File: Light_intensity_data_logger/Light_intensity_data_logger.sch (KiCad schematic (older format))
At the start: 12 parts

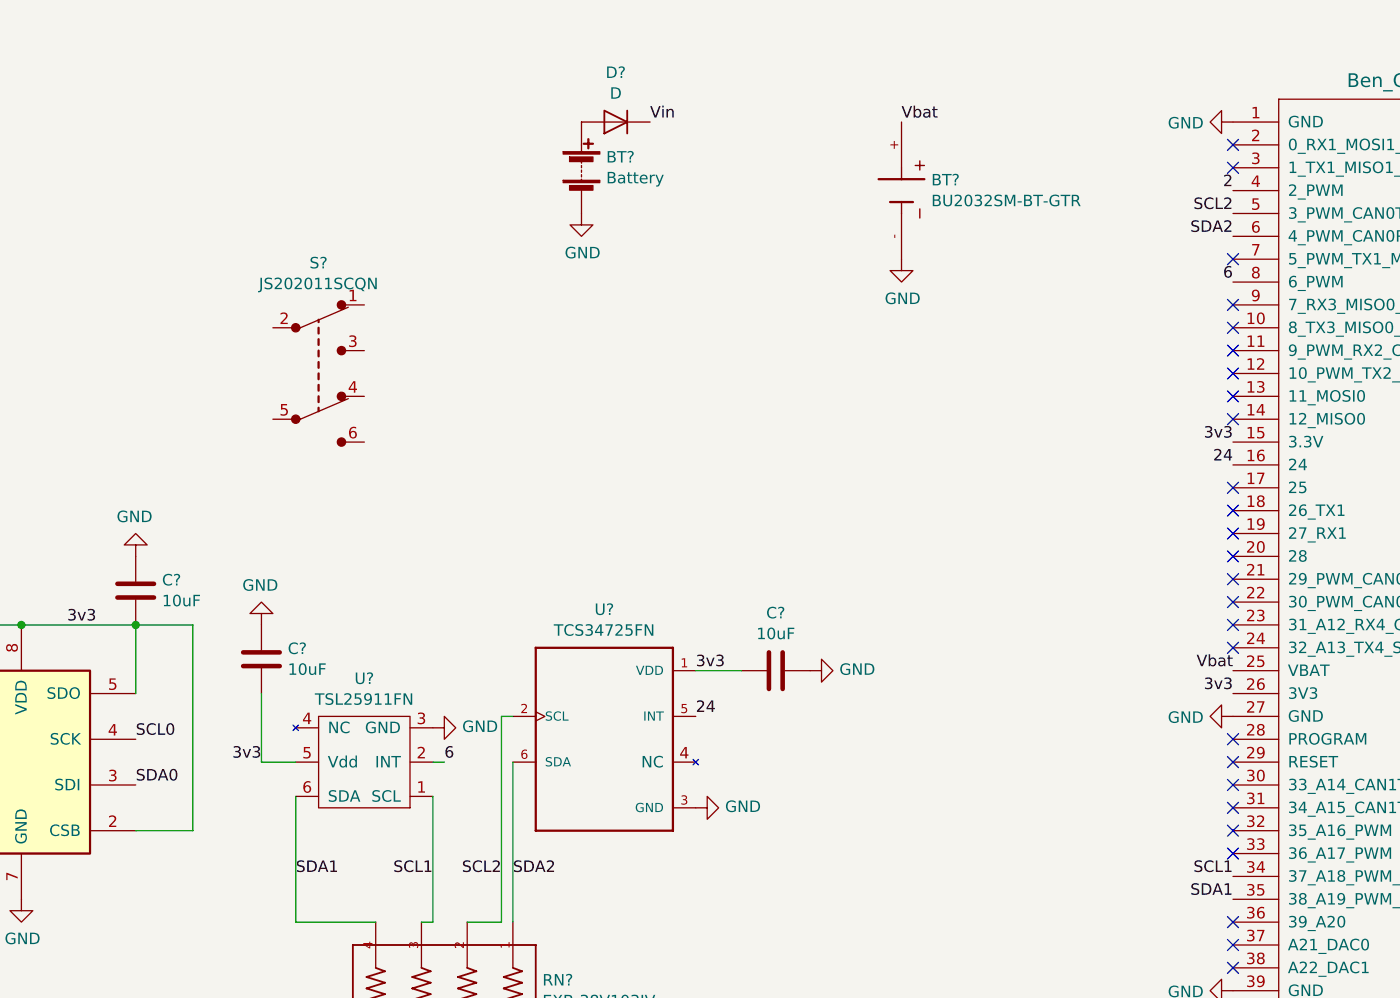
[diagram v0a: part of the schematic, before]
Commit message: Add power switch and Vbat sense
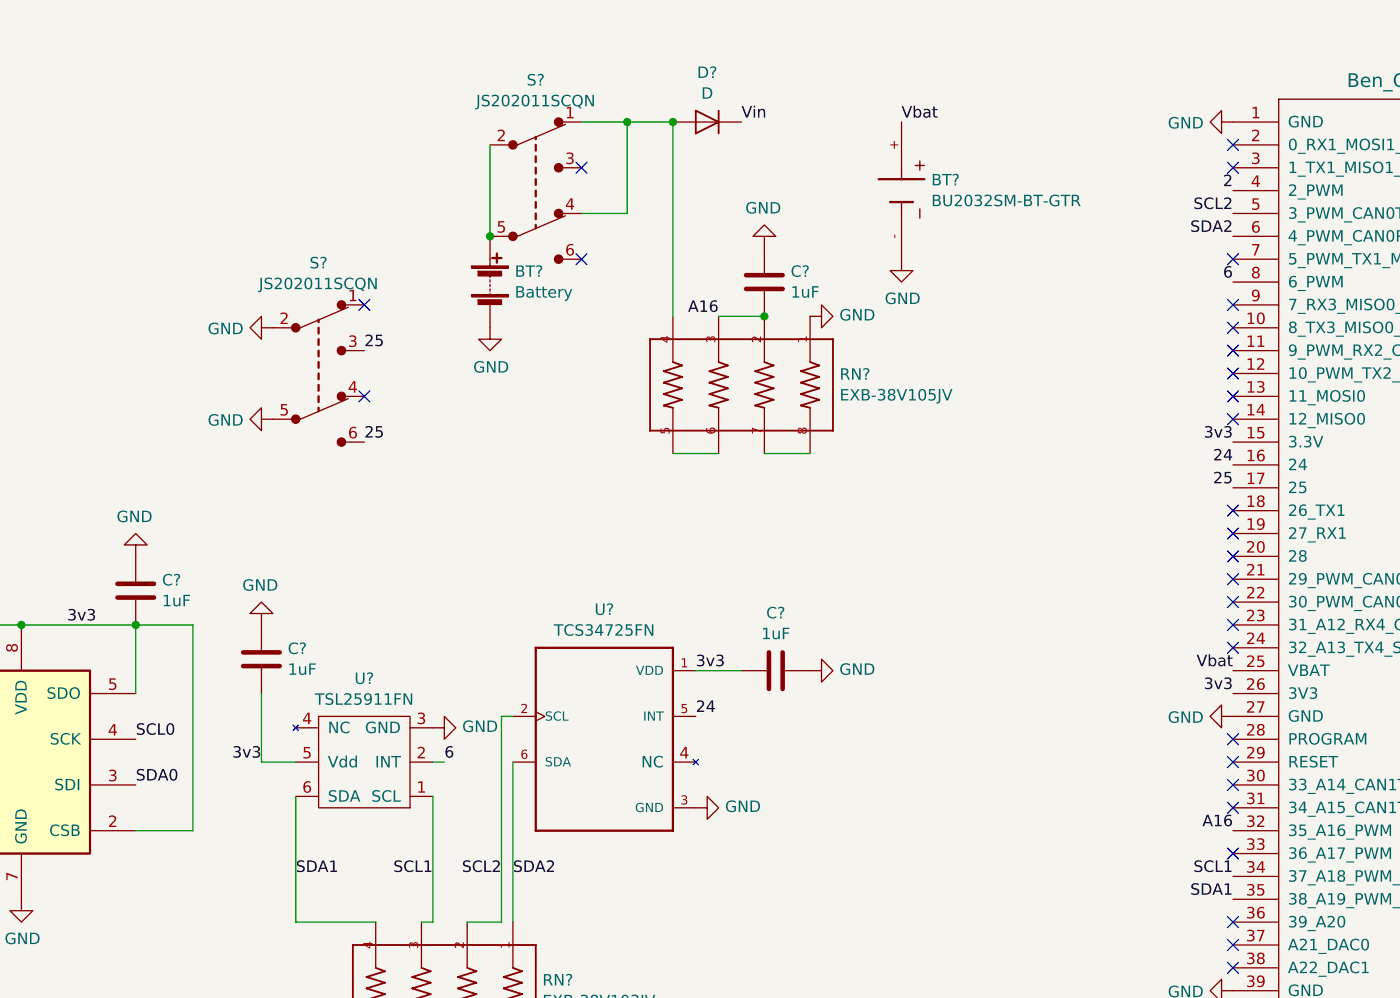
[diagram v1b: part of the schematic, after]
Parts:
- removed C? (x2): 10uF, Ben_Custom:0508_Capacitor, symbol device:C
- added C? (x3): 1uF, Capacitors_SMD:C_0603, symbol device:C
- added RN?: EXB-38V105JV, RESCAXS80P320X160X60-8N, symbol Ben_custom:EXB-38V103JV
- added S?: JS202011SCQN, digikey-footprints:Switch_Slide_JS202011SCQN, symbol dk_Slide-Switches:JS202011SCQN
- C?: value 10uF -> 1uF; footprint Ben_Custom:0508_Capacitor -> Capacitors_SMD:C_0603; Part# 587-5164-1-ND -> 1276-6524-1-ND
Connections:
- net 3v3: now also C?.2, C?.2
- net GND: now also S?.2, S?.5, C?.1, C?.1, C?.2, RN?.1
- net 25: now reaches U?.17 (25)
- net 25: now also S?.3, S?.6
- net A16: now reaches U?.32 (35_A16_PWM)
- net A16: now also C?.1, RN?.2, RN?.3
- net at BT?.1 (+): now also S?.2, S?.5; no longer D?.2 (A)
- new net: D?.2 (A), RN?.4, S?.1, S?.4
- new net: RN?.5, RN?.6
- new net: RN?.7, RN?.8
- no-connect marks 69 -> 71
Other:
- moved on the sheet: BT?, D?
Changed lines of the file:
@@
 L device:Battery BT?
 U 1 1 5E1E70C1
-P 5800 1050
-F 0 "BT?" H 5908 1096 50  0000 L CNN
-F 1 "Battery" H 5908 1005 50  0000 L CNN
-F 2 "Ben_Custom:BH3AAW-Battery_wire_pads" V 5800 1110 50  0001 C CNN
-F 3 "http://www.memoryprotectiondevices.com/datasheets/BH3AAW-datasheet.pdf" V 5800 1110 50  0001 C CNN
-F 4 "BH3AA-W-ND" H 5800 1050 50  0001 C CNN "Part#"
-	1    5800 1050
+P 5400 1550
+F 0 "BT?" H 5508 1596 50  0000 L CNN
+F 1 "Battery" H 5508 1505 50  0000 L CNN
+F 2 "Ben_Custom:BH3AAW-Battery_wire_pads" V 5400 1610 50  0001 C CNN
+F 3 "http://www.memoryprotectiondevices.com/datasheets/BH3AAW-datasheet.pdf" V 5400 1610 50  0001 C CNN
+F 4 "BH3AA-W-ND" H 5400 1550 50  0001 C CNN "Part#"
+	1    5400 1550
 	1    0    0    -1
 $EndComp
 Text Label 10950 4350 0    50   ~ 0
 Vin
-Text Label 6100 850  0    50   ~ 0
+Text Label 6500 850  0    50   ~ 0
 Vin
 $Comp
 L power:GND #PWR?
 U 1 1 5E1EC268
-P 5800 1250
-F 0 "#PWR?" H 5800 1000 50  0001 C CNN
-F 1 "GND" H 5805 1077 50  0000 C CNN
-F 2 "" H 5800 1250 50  0001 C CNN
-F 3 "" H 5800 1250 50  0001 C CNN
-	1    5800 1250
+P 5400 1750
+F 0 "#PWR?" H 5400 1500 50  0001 C CNN
+F 1 "GND" H 5405 1577 50  0000 C CNN
+F 2 "" H 5400 1750 50  0001 C CNN
+F 3 "" H 5400 1750 50  0001 C CNN
+	1    5400 1750
 	1    0    0    -1
 $EndComp
@@
 L device:D D?
 U 1 1 5E1F5931
-P 5950 850
-F 0 "D?" H 5950 634 50  0000 C CNN
-F 1 "D" H 5950 725 50  0000 C CNN
-F 2 "Diodes_SMD:D_SOD-323" H 5950 850 50  0001 C CNN
-F 3 "https://toshiba.semicon-storage.com/info/docget.jsp?did=14077&prodName=CUS10S30" H 5950 850 50  0001 C CNN
-F 4 "CUS10S30H3FCT-ND" H 5950 850 50  0001 C CNN "Part#"
-	1    5950 850
+P 6350 850
+F 0 "D?" H 6350 634 50  0000 C CNN
+F 1 "D" H 6350 725 50  0000 C CNN
+F 2 "Diodes_SMD:D_SOD-323" H 6350 850 50  0001 C CNN
+F 3 "https://toshiba.semicon-storage.com/info/docget.jsp?did=14077&prodName=CUS10S30" H 6350 850 50  0001 C CNN
+F 4 "CUS10S30H3FCT-ND" H 6350 850 50  0001 C CNN "Part#"
+	1    6350 850
 	-1   0    0    1
 $EndComp
@@
 F 1 "BME280" H 2821 3605 50  0000 R CNN
 F 2 "Housings_LGA:LGA-8_2.5x2.5mm_Pitch0.65mm" H 3250 3450 50  0001 C CNN
-F 3 "https://ae-bst.resource.bosch.com/media/_tech/media/datasheets/BST-BME280_DS001-11.pdf" H 3250 3450 50  0001 C CNN
+F 3 "https://www.bosch-sensortec.com/media/boschsensortec/downloads/environmental_sensors_2/humidity_sensors_1/bme280/bst-bme280-ds002.pdf" H 3250 3450 50  0001 C CNN
 F 4 "828-1063-1-ND" H 3250 3650 50  0001 C CNN "Part#"
 	1    3250 3650
@@
 NoConn ~ 8650 2050
 NoConn ~ 8650 2150
-NoConn ~ 8650 2450
 NoConn ~ 8650 2550
 NoConn ~ 8650 2650
@@
 NoConn ~ 8650 3750
 NoConn ~ 8650 3850
-NoConn ~ 8650 3950
 NoConn ~ 8650 4050
 NoConn ~ 8650 4350
@@
 P 3850 2900
 F 0 "C?" H 3965 2946 50  0000 L CNN
-F 1 "10uF" H 3965 2855 50  0000 L CNN
-F 2 "Ben_Custom:0508_Capacitor" H 3888 2750 50  0001 C CNN
-F 3 "https://media.digikey.com/pdf/Data%20Sheets/Taiyo%20Yuden%20PDFs%20URL%20links/EWK212BJ106MD-T_Spec.pdf" H 3850 2900 50  0001 C CNN
-F 4 "587-5164-1-ND" H 3850 2900 50  0001 C CNN "Part#"
+F 1 "1uF" H 3965 2855 50  0000 L CNN
+F 2 "Capacitors_SMD:C_0603" H 3888 2750 50  0001 C CNN
+F 3 "https://media.digikey.com/pdf/Data%20Sheets/Samsung%20PDFs/CL10B105MO8NNWC.pdf" H 3850 2900 50  0001 C CNN
+F 4 "1276-6524-1-ND" H 3850 2900 50  0001 C CNN "Part#"
 	1    3850 2900
 	1    0    0    -1
@@
 	-1   0    0    1
 $EndComp
-$Comp
-L device:C C?
-U 1 1 5E23E072
-P 4400 3200
-F 0 "C?" H 4515 3246 50  0000 L CNN
-F 1 "10uF" H 4515 3155 50  0000 L CNN
-F 2 "Ben_Custom:0508_Capacitor" H 4438 3050 50  0001 C CNN
-F 3 "https://media.digikey.com/pdf/Data%20Sheets/Taiyo%20Yuden%20PDFs%20URL%20links/EWK212BJ106MD-T_Spec.pdf" H 4400 3200 50  0001 C CNN
-F 4 "587-5164-1-ND" H 4400 3200 50  0001 C CNN "Part#"
-	1    4400 3200
-	1    0    0    -1
-$EndComp
 Wire Wire Line
 	4550 3650 4400 3650
@@
 	1    4400 3050
 	-1   0    0    1
-$EndComp
-$Comp
-L device:C C?
-U 1 1 5E23FF0F
-P 6650 3250
-F 0 "C?" V 6398 3250 50  0000 C CNN
-F 1 "10uF" V 6489 3250 50  0000 C CNN
-F 2 "Ben_Custom:0508_Capacitor" H 6688 3100 50  0001 C CNN
-F 3 "https://media.digikey.com/pdf/Data%20Sheets/Taiyo%20Yuden%20PDFs%20URL%20links/EWK212BJ106MD-T_Spec.pdf" H 6650 3250 50  0001 C CNN
-F 4 "587-5164-1-ND" H 6650 3250 50  0001 C CNN "Part#"
-	1    6650 3250
-	0    1    1    0
 $EndComp
 Wire Wire Line
@@
 Wire Wire Line
 	4100 3950 3850 3950
+$Comp
+L device:C C?
+U 1 1 5E24F840
+P 4400 3200
+F 0 "C?" H 4515 3246 50  0000 L CNN
+F 1 "1uF" H 4515 3155 50  0000 L CNN
+F 2 "Capacitors_SMD:C_0603" H 4438 3050 50  0001 C CNN
+F 3 "https://media.digikey.com/pdf/Data%20Sheets/Samsung%20PDFs/CL10B105MO8NNWC.pdf" H 4400 3200 50  0001 C CNN
+F 4 "1276-6524-1-ND" H 4400 3200 50  0001 C CNN "Part#"
+	1    4400 3200
+	1    0    0    -1
+$EndComp
+$Comp
+L device:C C?
+U 1 1 5E24FD3B
+P 6650 3250
+F 0 "C?" V 6398 3250 50  0000 C CNN
+F 1 "1uF" V 6489 3250 50  0000 C CNN
+F 2 "Capacitors_SMD:C_0603" H 6688 3100 50  0001 C CNN
+F 3 "https://media.digikey.com/pdf/Data%20Sheets/Samsung%20PDFs/CL10B105MO8NNWC.pdf" H 6650 3250 50  0001 C CNN
+F 4 "1276-6524-1-ND" H 6650 3250 50  0001 C CNN "Part#"
+	1    6650 3250
+	0    1    1    0
+$EndComp
+$Comp
+L Ben_custom:EXB-38V103JV RN?
+U 1 1 5E251FAC
+P 6500 2000
+F 0 "RN?" V 6454 2429 50  0000 L CNN
+F 1 "EXB-38V105JV" V 6545 2429 50  0000 L CNN
+F 2 "RESCAXS80P320X160X60-8N" H 6500 2000 50  0001 L BNN
+F 3 "https://media.digikey.com/pdf/Data%20Sheets/Panasonic%20Resistors%20Thermistors%20PDFs/EXB38V%20Spec.pdf" H 6500 2000 50  0001 L BNN
+F 4 "Y9105CT-ND" H 6500 2000 50  0001 L BNN "Part#"
+	1    6500 2000
+	0    1    1    0
+$EndComp
+Wire Wire Line
+	6200 850  6000 850
+Wire Wire Line
+	6200 850  6200 1700
+Connection ~ 6200 850
+Wire Wire Line
+	6200 2300 6400 2300
+Wire Wire Line
+	6600 2300 6800 2300
+$Comp
+L power:GND #PWR?
+U 1 1 5E2599BD
+P 6800 1700
+F 0 "#PWR?" H 6800 1450 50  0001 C CNN
+F 1 "GND" V 6805 1572 50  0000 R CNN
+F 2 "" H 6800 1700 50  0001 C CNN
+F 3 "" H 6800 1700 50  0001 C CNN
+	1    6800 1700
+	0    -1   -1   0
+$EndComp
+$Comp
+L device:C C?
+U 1 1 5E259F31
+P 6600 1550
+F 0 "C?" H 6485 1504 50  0000 R CNN
+F 1 "1uF" H 6485 1595 50  0000 R CNN
+F 2 "Capacitors_SMD:C_0603" H 6638 1400 50  0001 C CNN
+F 3 "https://media.digikey.com/pdf/Data%20Sheets/Samsung%20PDFs/CL10B105MO8NNWC.pdf" H 6600 1550 50  0001 C CNN
+F 4 "1276-6524-1-ND" H 6600 1550 50  0001 C CNN "Part#"
+	1    6600 1550
+	-1   0    0    1
+$EndComp
+$Comp
+L power:GND #PWR?
+U 1 1 5E25A6EE
+P 6600 1400
+F 0 "#PWR?" H 6600 1150 50  0001 C CNN
+F 1 "GND" H 6605 1227 50  0000 C CNN
+F 2 "" H 6600 1400 50  0001 C CNN
+F 3 "" H 6600 1400 50  0001 C CNN
+	1    6600 1400
+	-1   0    0    1
+$EndComp
+Connection ~ 6600 1700
+Wire Wire Line
+	6400 1700 6600 1700
+Text Label 8650 3950 2    50   ~ 0
+A16
+Text Label 6400 1700 2    50   ~ 0
+A16
+Text Label 8650 2450 2    50   ~ 0
+25
+Text Label 4850 1850 0    50   ~ 0
+25
+Text Label 4850 2250 0    50   ~ 0
+25
+$Comp
+L power:GND #PWR?
+U 1 1 5E25E1DF
+P 4450 1750
+F 0 "#PWR?" H 4450 1500 50  0001 C CNN
+F 1 "GND" V 4455 1622 50  0000 R CNN
+F 2 "" H 4450 1750 50  0001 C CNN
+F 3 "" H 4450 1750 50  0001 C CNN
+	1    4450 1750
+	0    1    1    0
+$EndComp
+$Comp
+L power:GND #PWR?
+U 1 1 5E25ED59
+P 4450 2150
+F 0 "#PWR?" H 4450 1900 50  0001 C CNN
+F 1 "GND" V 4455 2022 50  0000 R CNN
+F 2 "" H 4450 2150 50  0001 C CNN
+F 3 "" H 4450 2150 50  0001 C CNN
+	1    4450 2150
+	0    1    1    0
+$EndComp
+NoConn ~ 4850 1650
+NoConn ~ 4850 2050
+$Comp
+L dk_Slide-Switches:JS202011SCQN S?
+U 1 1 5E261D45
+P 5600 1150
+F 0 "S?" H 5600 1633 50  0000 C CNN
+F 1 "JS202011SCQN" H 5600 1542 50  0000 C CNN
+F 2 "digikey-footprints:Switch_Slide_JS202011SCQN" H 5800 1350 50  0001 L CNN
+F 3 "https://www.ckswitches.com/media/1422/js.pdf" H 5800 1450 60  0001 L CNN
+F 4 "401-2002-1-ND" H 5800 2350 60  0001 L CNN "Part#"
+	1    5600 1150
+	1    0    0    -1
+$EndComp
+Wire Wire Line
+	6000 850  6000 1250
+Wire Wire Line
+	6000 1250 5800 1250
+Connection ~ 6000 850
+Wire Wire Line
+	6000 850  5800 850
+NoConn ~ 5800 1050
+NoConn ~ 5800 1450
+Wire Wire Line
+	5400 950  5400 1350
+Connection ~ 5400 1350
 $EndSCHEMATC
